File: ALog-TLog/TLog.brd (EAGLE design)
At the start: 124.1 x 45.3 mm, 102 parts, among them IC1 ATMEGA644M, J6 5.5x2.1mm Barrel, Q1 MOSFET-NCH-BSS138, Q5 MOSFET_PCH-IRLML2244, Q6 MOSFET_PCH-IRLML2244, Q7 MOSFET_PCH-IRLML2244, Q8 MOSFET-NCH-BSS138, Q9 MOSFET-NCH-BSS138, U2 FT231X-Q, U3 915MHz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

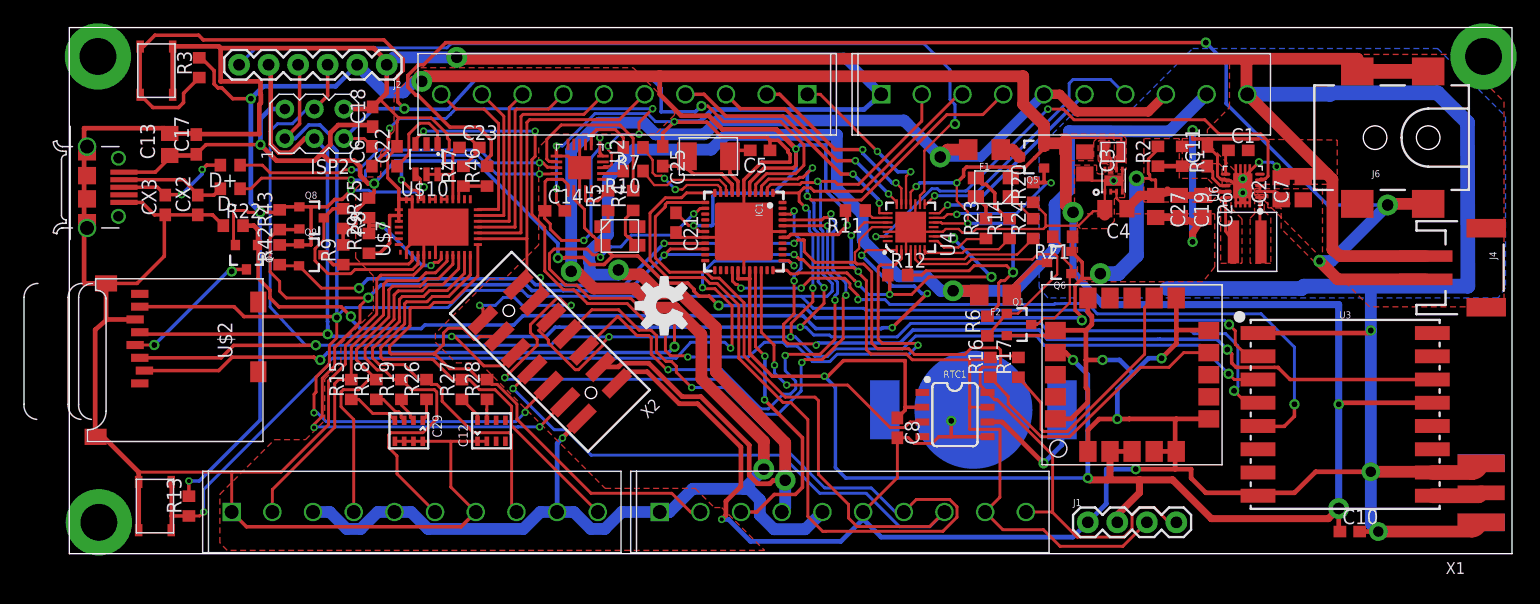
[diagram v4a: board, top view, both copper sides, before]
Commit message: Added Gate Drivers, Fixed Basic Issues
Added gate drievrs to all MOSFETs, also broke out battery voltage to screw terminals, and increased size of push button pads to improve reflow
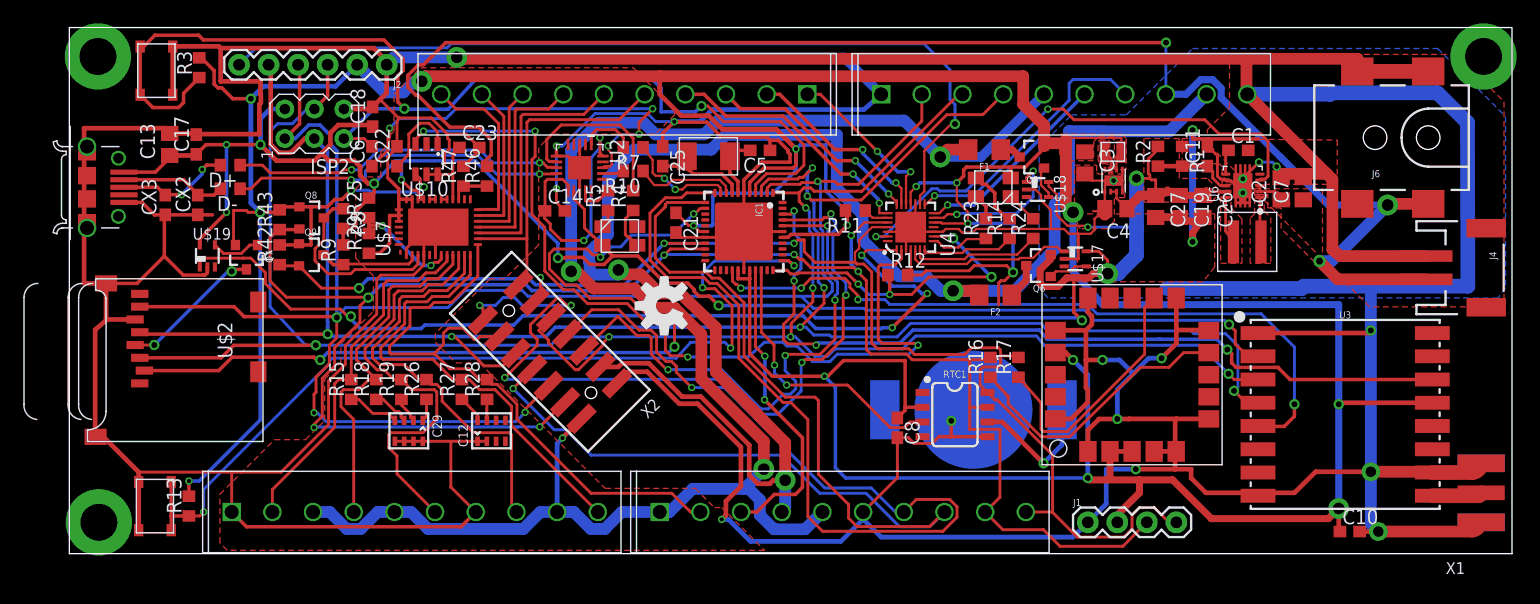
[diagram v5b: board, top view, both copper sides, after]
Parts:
- removed Q1: MOSFET-NCH-BSS138, bschulz:SOT23-3
- removed R20, R21, R22: 10k, bschulz:R0603
- removed R6: (no value), bschulz:R0603
- added U$17, U$18, U$19: MIC842, bschulz:DCK_R-PDSO-G5
- U$5, U$9: value SWITCHC&K_400GF -> BUTTON4.2X3.2
- moved Q6 1.80 mm to (83.6, 24.9)
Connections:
- new net N$1: Q5.1, U$18.4
- new net N$3: Q7.1, U$19.4
- net 3.3V_EXT_CTRL: now also U$18.1; no longer Q5.1, R20.2
- net 3V3: no longer R6.2
- net 5V: now also U$17.5, U$18.5, U$19.5; no longer R21.1
- net 5V_EXT_CTRL: now also U$17.1; no longer Q1.1, R6.1
- net BATT: now also J10.P$8
- net EXT_3.3V: no longer J10.P$8
- net GND: now also U$17.2, U$18.2, U$19.2, U$5.1, U$5.2, U$9.1, U$9.2; no longer Q1.2, R20.1, R22.1, U$5.P$1, U$5.P$2, U$9.P$1, U$9.P$2
- net LOG_INT: now also U$5.3, U$5.4; no longer U$5.P$3, U$5.P$4
- net N$30: now also U$17.4; no longer Q1.3, R21.2
- net RST: now also U$9.3, U$9.4; no longer U$9.P$3, U$9.P$4
- net SD_VCC_CTRL: now also U$19.1; no longer Q7.1, R22.2
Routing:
- net 5V: track 161.9 -> 187.9 mm, vias 8 -> 11
- net EXT_3.3V: track 160.6 -> 148.8 mm
- net 5V_EXT_CTRL: track 23.4 -> 14.5 mm
- net GND: track 833.3 -> 840.8 mm
- net N$30: track 10.8 -> 3.42 mm
- net N$3: track 0.00 -> 4.27 mm
- net N$1: track 0.00 -> 2.87 mm
- net 3.3V_EXT_CTRL: track 15.2 -> 12.8 mm
- net BATT: track 130.7 -> 132.8 mm
- net 3V3: track 432.6 -> 431.2 mm
- net N$18: track 4.52 -> 3.63 mm
- net SD_VCC_CTRL: track 77.9 -> 78.8 mm
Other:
- board text added: "BAT"
